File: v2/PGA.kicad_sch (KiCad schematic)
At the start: 15 parts, among them U15 OPA333xxD, U17 PGA113, U24 TLV9061xDBV

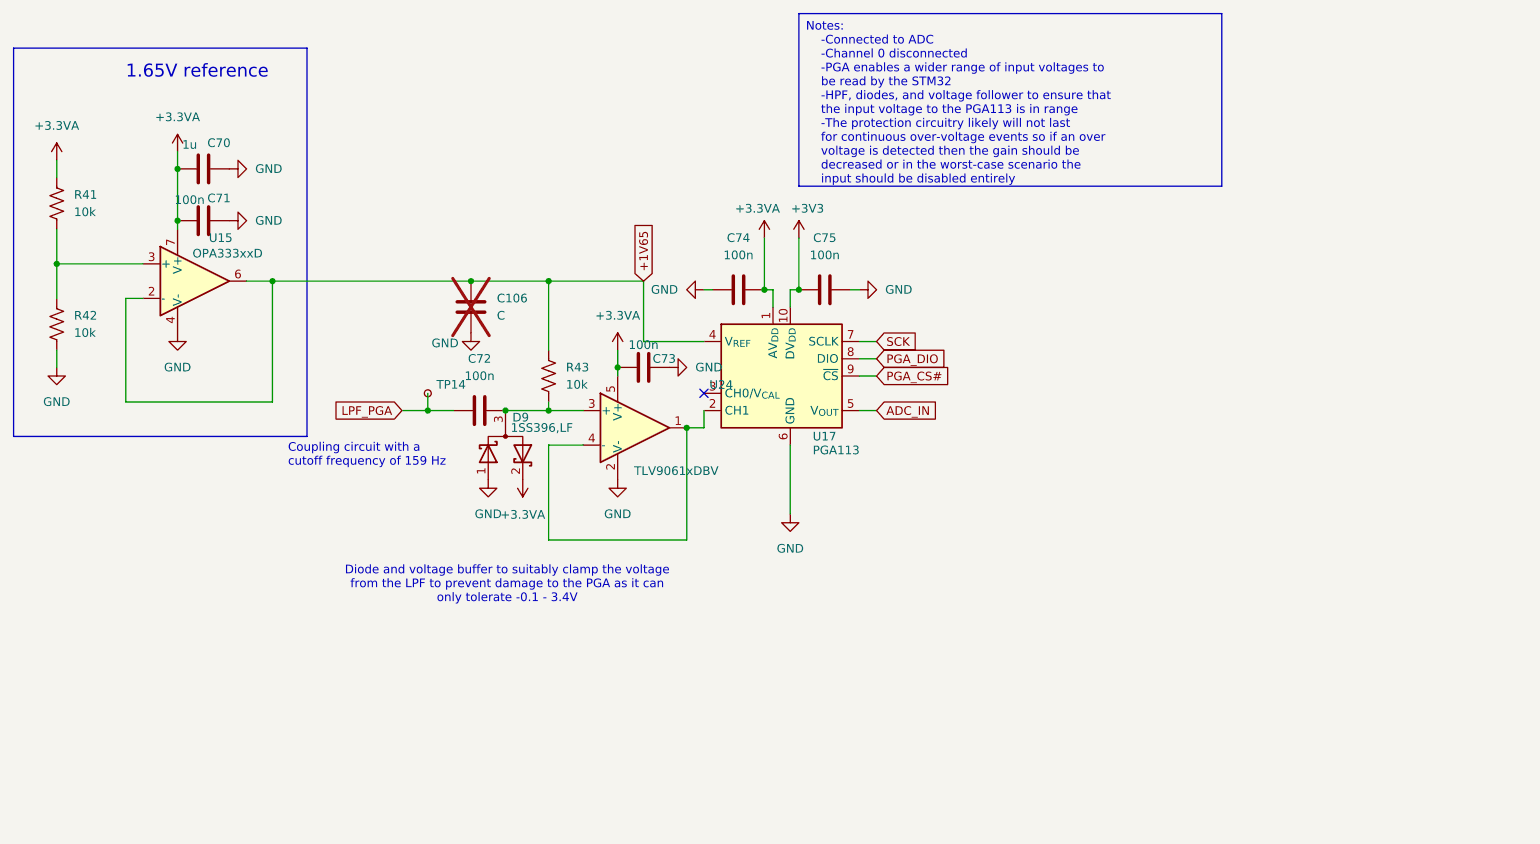
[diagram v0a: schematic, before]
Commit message: Most v2 changes made
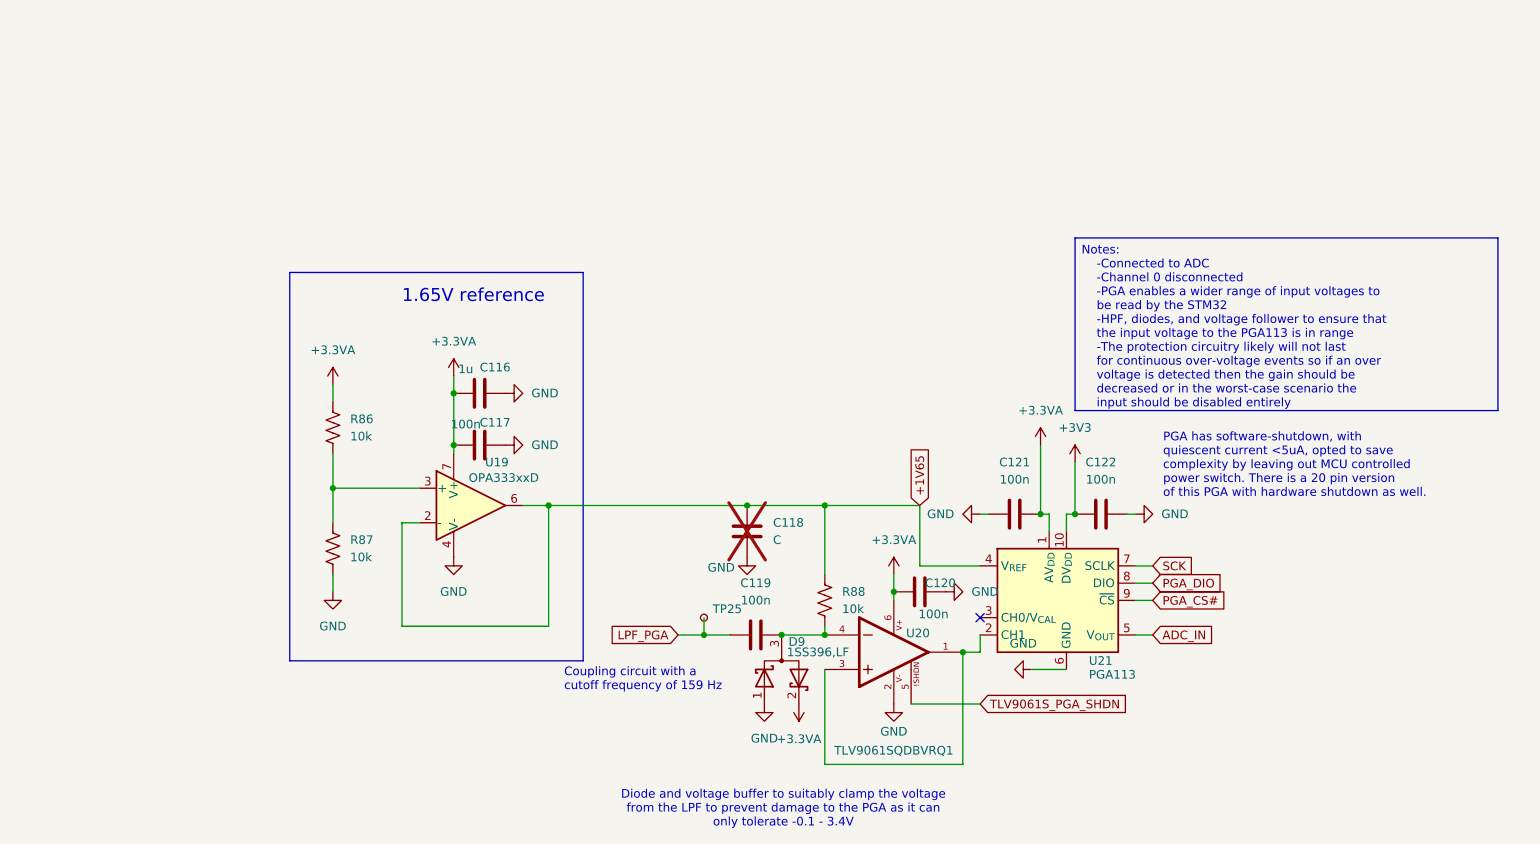
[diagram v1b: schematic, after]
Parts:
- removed R41, R42, R43: 10k, Resistor_SMD:R_0603_1608Metric_Pad0.98x0.95mm_HandSolder, symbol UAM_symbols:R_US
- removed U24: TLV9061xDBV, Package_TO_SOT_SMD:SOT-23-5, symbol UAM_symbols:TLV9061xDBV
- added R86, R87, R88: 10k, Resistor_SMD:R_0603_1608Metric_Pad0.98x0.95mm_HandSolder, symbol UAM_symbols:R_US
- added U20: TLV9061SQDBVRQ1, UAM_footprints:SOT95P280X145-6N, symbol UAM_symbols:TLV9061SQDBVRQ1
- renumbered C70 to C116, C71 to C117, C106 to C118, C72 to C119, C73 to C120, C74 to C121, C75 to C122, TP14 to TP25, U15 to U19, U17 to U21
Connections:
- net +1V65: now also R88.1
- net +3.3VA: now also R86.1, U20.6
- net GND: now also R87.2, U20.2
- net at C119.2, D9.3 (A): now also R88.2, U20.4
- net at U19.3 (+): now also R86.2, R87.1
- net at U21.2 (CH1): now also U20.1, U20.3
- new net TLV9061S_PGA_SHDN: U20.5
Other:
- note added: "PGA has software-shutdown, with quiescent current <5uA, opted to save complexity by leaving out MCU controlled power switch. There is a 20 pin version of this PGA with hardware shutdown as well."
- company: Programmable Gain Amplifier -> (none)
- title: RM -> (none)
- moved on the sheet: C116, C117, C118, C119, C120, C121, C122, D9, TP25, U19, U21
